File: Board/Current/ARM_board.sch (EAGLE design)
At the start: 168 parts, among them IC3 STM32F437VI, IC4 LM358DT, J1 USART/I2C, J10 ANALOG, J11 DGND, J12 DPWR, J13 DIGITAL, J14 SGND, J15 SPWR, J16 SERVO, J2 I2C2/USART3, J3 USART2, J5 SPI, J6 Bluesmirf, J7 SWD, J8 AGND, J9 APWR, Q1 STL4P2UH7, Q2 2STR1230, SW1 SW, U1 LSM330DLC, U10 BAV99, U11 BAV99, U12 USBLC6-2, U13 USBLC6-2, U14 STMPS2171MTR, U15 MC74HC164, U17 ?, U18 ?, U19 ?, U20 ?, U3 NC7SZU04, U4 L6206Q, U5 L6206Q, U6 SI7617, U7 SI7617, U8 SI7617, U9 SI7617, Y2 8MHz

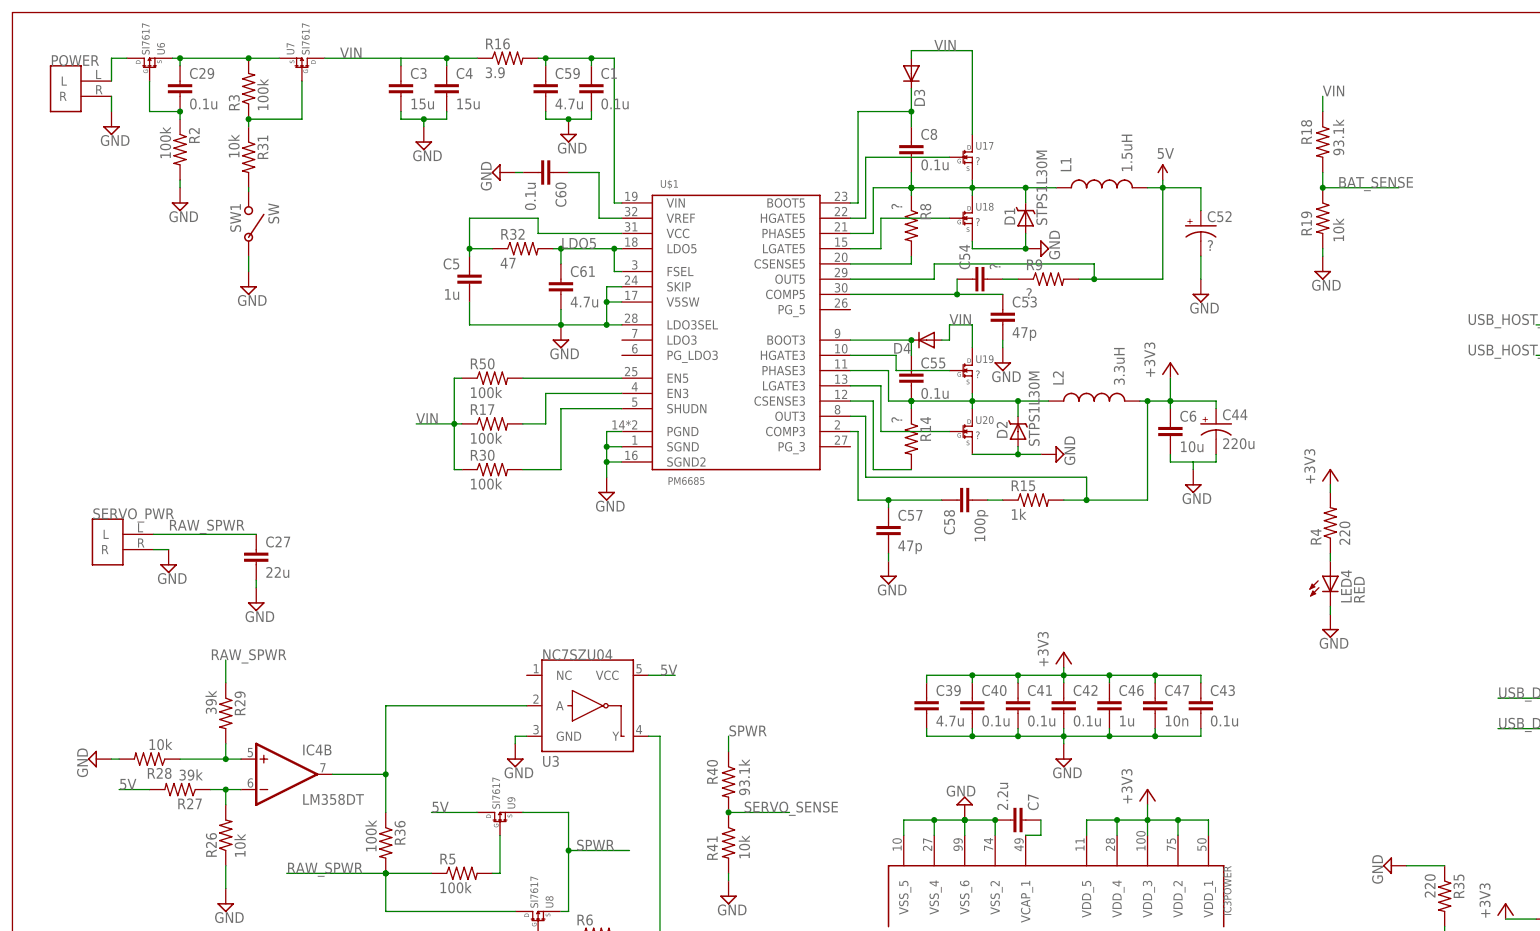
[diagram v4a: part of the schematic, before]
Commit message: Made changes to switching regulator section of schematic.
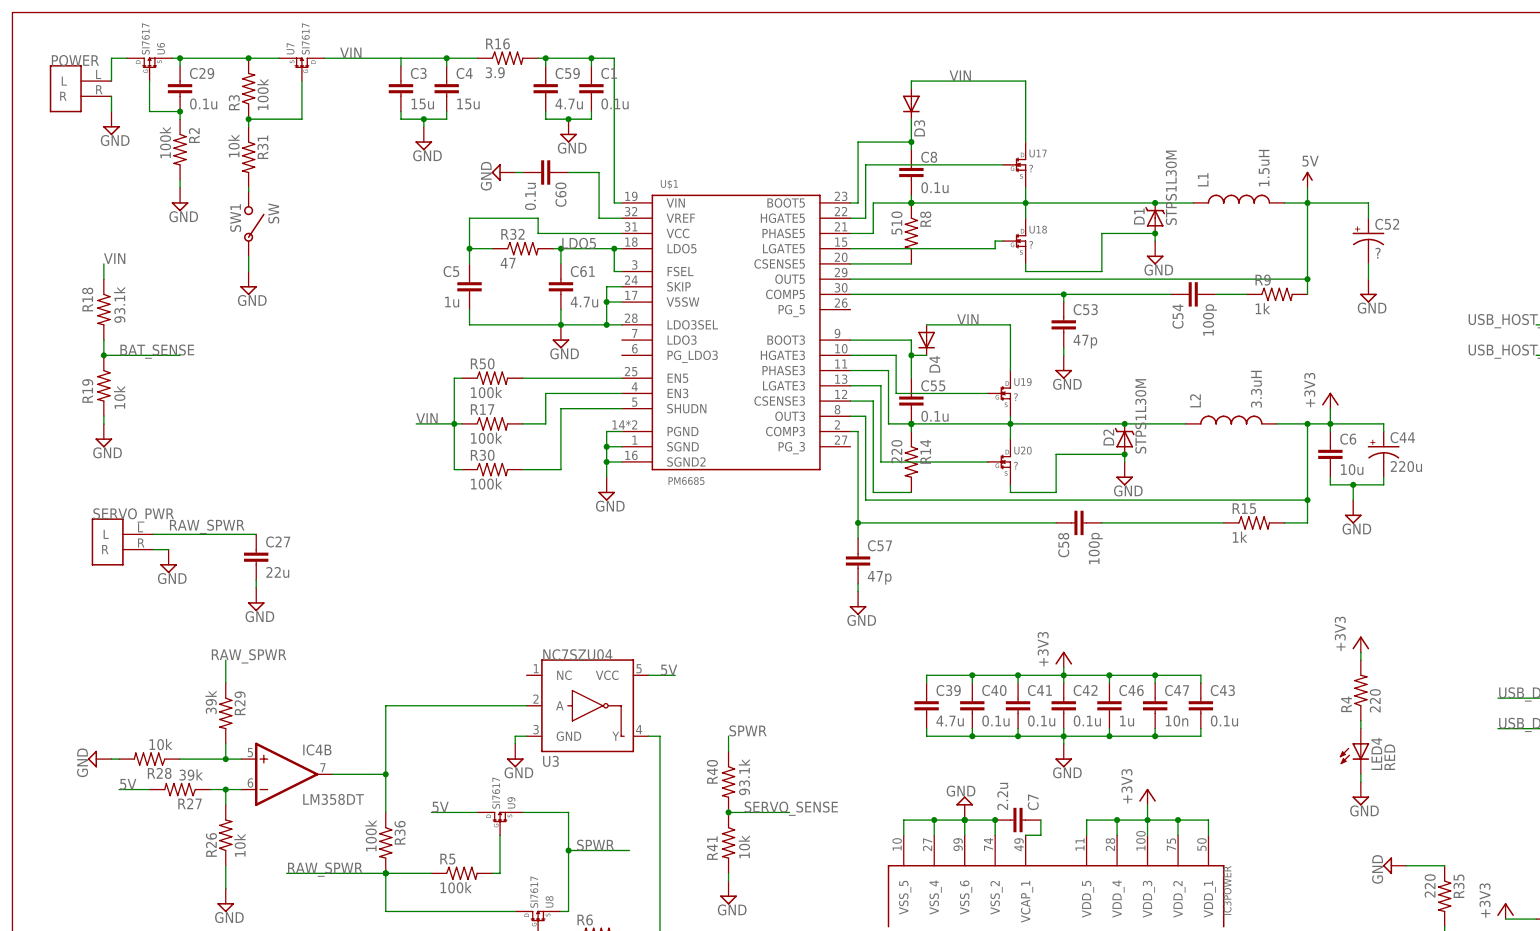
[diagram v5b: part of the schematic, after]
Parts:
- C54: value ? -> 100p
- R14: value ? -> 220
- R8: value ? -> 510
- R9: value ? -> 1k
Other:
- moved on the sheet: C44, C5, C52, C53, C54, C55, C57, C58, C6, C8, D1, D2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

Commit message: Created parts for Issue 44
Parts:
- removed D4: (no value), SparkFun:DIODESMA
- removed L2: 3.3uH, r_cubed:INDUCTOR
- added L3: 3.3uH, r_cubed:INDUCTOR3
- added U$2: DUAL-MOSFET, r_cubed:DUAL-MOSFET
- D1, D2: device SparkFun:DIODE-SCHOTTKY_ -> SparkFun:DIODE-SCHOTTKYA
- D3: value (none) -> SOD-23; device SparkFun:DIODESMA -> r_cubed:SOD-23
- L1: device r_cubed:INDUCTOR -> r_cubed:INDUCTOR2
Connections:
- net +3V3: now also L3.2; no longer L2.2
- net N$25: now also D3.P$1; no longer D3.C
- net N$74: now also D3.P$2; no longer D4.C
- net N$75: now also L3.1; no longer L2.1
- net VIN: now also D3.P$0; no longer D3.A, D4.A
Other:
- note added: "D3"
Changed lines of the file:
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@@
 <?xml version="1.0" encoding="utf-8"?>
 <!DOCTYPE eagle SYSTEM "eagle.dtd">
-<eagle version="6.3">
+<eagle version="6.5.0">
 <drawing>
 <settings>
@@
 <setting verticaltext="up"/>
 </settings>
-<grid distance="0.05" unitdist="inch" unit="inch" style="lines" multiple="1" display="no" altdistance="0.01" altunitdist="inch" altunit="inch"/>
+<grid distance="0.1" unitdist="inch" unit="inch" style="lines" multiple="1" display="no" altdistance="0.01" altunitdist="inch" altunit="inch"/>
 <layers>
 <layer number="1" name="Top" color="4" fill="1" visible="no" active="no"/>
@@
 <part name="SUPPLY49" library="supply2" deviceset="GND" device=""/>
 <part name="U17" library="r_cubed" deviceset="STL85N6F3" device="" value="?"/>
-<part name="L1" library="r_cubed" deviceset="INDUCTOR" device="" value="1.5uH"/>
+<part name="L1" library="r_cubed" deviceset="INDUCTOR" device="2" value="1.5uH"/>
 <part name="U18" library="r_cubed" deviceset="STL85N6F3" device="" value="?"/>
 <part name="SUPPLY58" library="supply2" deviceset="GND" device=""/>
@@
 <part name="SUPPLY60" library="supply2" deviceset="GND" device=""/>
 <part name="R9" library="SparkFun" deviceset="RESISTOR" device="0402-RES" value="1k"/>
-<part name="D1" library="SparkFun" deviceset="DIODE-SCHOTTKY" device="_" value="STPS1L30M"/>
+<part name="D1" library="SparkFun" deviceset="DIODE-SCHOTTKY" device="A" value="STPS1L30M"/>
 <part name="U19" library="r_cubed" deviceset="STL85N6F3" device="" value="?"/>
-<part name="L2" library="r_cubed" deviceset="INDUCTOR" device="" value="3.3uH"/>
 <part name="U20" library="r_cubed" deviceset="STL85N6F3" device="" value="?"/>
 <part name="C55" library="SparkFun" deviceset="CAP" device="0402-CAP" value="0.1u"/>
@@
 <part name="SUPPLY67" library="supply2" deviceset="GND" device=""/>
 <part name="R15" library="SparkFun" deviceset="RESISTOR" device="0402-RES" value="1k"/>
-<part name="D2" library="SparkFun" deviceset="DIODE-SCHOTTKY" device="_" value="STPS1L30M"/>
-<part name="D3" library="SparkFun" deviceset="DIODE" device="SMA"/>
-<part name="D4" library="SparkFun" deviceset="DIODE" device="SMA"/>
+<part name="D2" library="SparkFun" deviceset="DIODE-SCHOTTKY" device="A" value="STPS1L30M"/>
 <part name="R16" library="SparkFun" deviceset="RESISTOR" device="0402-RES" value="3.9"/>
 <part name="C59" library="SparkFun" deviceset="CAP" device="0402-CAP" value="4.7u"/>
@@
 <part name="C8" library="SparkFun" deviceset="CAP" device="0402-CAP" value="0.1u"/>
 <part name="SUPPLY71" library="supply2" deviceset="GND" device=""/>
+<part name="L3" library="r_cubed" deviceset="INDUCTOR" device="3" value="3.3uH"/>
+<part name="D3" library="r_cubed" deviceset="SOD-23" device=""/>
+<part name="U$2" library="r_cubed" deviceset="DUAL-MOSFET" device=""/>
 </parts>
 <sheets>
@@
 <wire x1="455.93" y1="0" x2="0" y2="0" width="0.1524" layer="94"/>
 <wire x1="0" y1="0" x2="0" y2="309.88" width="0.1524" layer="94"/>
+<text x="156.21" y="299.466" size="1.778" layer="95" rot="R180">D3</text>
 </plain>
 <instances>
@@
 </instance>
 <instance part="U19" gate="G$1" x="167.64" y="246.38"/>
-<instance part="L2" gate="G$1" x="203.2" y="241.3" rot="R90"/>
 <instance part="U20" gate="G$1" x="167.64" y="234.95"/>
 <instance part="C55" gate="G$1" x="149.86" y="243.84"/>
@@
 <attribute name="VALUE" x="189.0014" y="236.22" size="1.778" layer="96" rot="R90"/>
 </instance>
-<instance part="D3" gate="G$1" x="149.86" y="294.64" rot="R270"/>
-<instance part="D4" gate="G$1" x="152.4" y="255.27" rot="R270"/>
 <instance part="R16" gate="G$1" x="82.55" y="302.26"/>
 <instance part="C59" gate="G$1" x="88.9" y="295.91"/>
@@
 <instance part="C8" gate="G$1" x="149.86" y="281.94"/>
 <instance part="SUPPLY71" gate="GND" x="190.5" y="269.24"/>
+<instance part="L3" gate="G$1" x="203.2" y="241.3" rot="R90"/>
+<instance part="D3" gate="G$1" x="159.004" y="300.99"/>
+<instance part="U$2" gate="G$1" x="185.42" y="297.18"/>
 </instances>
 <busses>
@@
 <pinref part="U17" gate="G$1" pin="D"/>
 <wire x1="168.91" y1="288.29" x2="168.91" y2="298.45" width="0.1524" layer="91"/>
-<label x="156.21" y="298.45" size="1.778" layer="95"/>
-<pinref part="D3" gate="G$1" pin="A"/>
-<wire x1="168.91" y1="298.45" x2="149.86" y2="298.45" width="0.1524" layer="91"/>
-<wire x1="149.86" y1="298.45" x2="149.86" y2="297.18" width="0.1524" layer="91"/>
+<wire x1="168.91" y1="298.45" x2="164.084" y2="298.45" width="0.1524" layer="91"/>
+<pinref part="D3" gate="G$1" pin="P$0"/>
+<label x="167.132" y="298.704" size="1.778" layer="95"/>
 </segment>
 <segment>
 <pinref part="U19" gate="G$1" pin="D"/>
 <wire x1="166.37" y1="250.19" x2="166.37" y2="257.81" width="0.1524" layer="91"/>
-<wire x1="166.37" y1="257.81" x2="152.4" y2="257.81" width="0.1524" layer="91"/>
-<label x="157.48" y="257.81" size="1.778" layer="95"/>
-<pinref part="D4" gate="G$1" pin="A"/>
+<label x="164.084" y="258.064" size="1.778" layer="95"/>
 </segment>
 <segment>
@@
 </segment>
 <segment>
-<pinref part="L2" gate="G$1" pin="2"/>
 <wire x1="210.82" y1="241.3" x2="215.9" y2="241.3" width="0.1524" layer="91"/>
 <junction x="215.9" y="241.3"/>
@@
 <pinref part="+3V1" gate="G$1" pin="+3V3"/>
 <wire x1="219.71" y1="243.84" x2="219.71" y2="241.3" width="0.1524" layer="91"/>
+<pinref part="L3" gate="G$1" pin="2"/>
 </segment>
 </net>
@@
 <wire x1="152.4" y1="252.73" x2="149.86" y2="252.73" width="0.1524" layer="91"/>
 <pinref part="U$1" gate="G$1" pin="BOOT3"/>
-<pinref part="D4" gate="G$1" pin="C"/>
 <pinref part="C55" gate="G$1" pin="1"/>
 <wire x1="149.86" y1="252.73" x2="149.86" y2="255.27" width="0.1524" layer="91"/>
@@
 <wire x1="149.86" y1="252.73" x2="149.86" y2="248.92" width="0.1524" layer="91"/>
 <junction x="149.86" y="252.73"/>
+<label x="153.162" y="252.73" size="1.778" layer="95"/>
+</segment>
+<segment>
+<pinref part="D3" gate="G$1" pin="P$2"/>
+<wire x1="159.004" y1="290.83" x2="159.004" y2="289.052" width="0.1524" layer="91"/>
+<label x="156.464" y="286.766" size="1.778" layer="95"/>
 </segment>
 </net>
@@
 <wire x1="166.37" y1="241.3" x2="166.37" y2="242.57" width="0.1524" layer="91"/>
 <junction x="166.37" y="241.3"/>
-<pinref part="L2" gate="G$1" pin="1"/>
 <wire x1="195.58" y1="241.3" x2="185.42" y2="241.3" width="0.1524" layer="91"/>
 <wire x1="166.37" y1="241.3" x2="185.42" y2="241.3" width="0.1524" layer="91"/>
@@
 <pinref part="D2" gate="G$1" pin="C"/>
 <pinref part="U$1" gate="G$1" pin="PHASE3"/>
+<pinref part="L3" gate="G$1" pin="1"/>
 </segment>
 </net>
@@
 <net name="N$25" class="0">
 <segment>
-<pinref part="D3" gate="G$1" pin="C"/>
 <wire x1="149.86" y1="287.02" x2="149.86" y2="288.29" width="0.1524" layer="91"/>
 <pinref part="C8" gate="G$1" pin="1"/>
-<wire x1="149.86" y1="288.29" x2="149.86" y2="292.1" width="0.1524" layer="91"/>
 <junction x="149.86" y="288.29"/>
 <pinref part="U$1" gate="G$1" pin="BOOT5"/>
@@
 <wire x1="149.86" y1="288.29" x2="140.97" y2="288.29" width="0.1524" layer="91"/>
 <wire x1="140.97" y1="288.29" x2="140.97" y2="278.13" width="0.1524" layer="91"/>
+<pinref part="D3" gate="G$1" pin="P$1"/>
+<wire x1="159.004" y1="306.07" x2="149.86" y2="306.07" width="0.1524" layer="91"/>
+<wire x1="149.86" y1="306.07" x2="149.86" y2="288.29" width="0.1524" layer="91"/>
 </segment>
 </net>
